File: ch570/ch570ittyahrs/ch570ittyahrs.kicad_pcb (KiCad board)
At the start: 2 copper layers, 0 parts

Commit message: Bump design
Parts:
- added C1: 4.7u, Capacitor_SMD:C_0402_1005Metric, F.Cu at (114.0, 45.3)
- added C10: 0.1μF, Capacitor_SMD:C_0402_1005Metric, F.Cu at (79.9, 59.0)
- added C12: 22μF, Capacitor_SMD:C_0603_1608Metric, F.Cu at (73.6, 57.8)
- added C13: 0.1μF, Capacitor_SMD:C_0402_1005Metric, F.Cu at (79.9, 60.9)
- added C14: 22pF, Capacitor_SMD:C_0402_1005Metric, F.Cu at (79.9, 62.9)
- added C2: 4.7u, Capacitor_SMD:C_0402_1005Metric, F.Cu at (77.0, 57.0)
- added C3: 4.7u, Capacitor_SMD:C_0402_1005Metric, F.Cu at (77.0, 59.0)
- added C4: 0.1u, Capacitor_SMD:C_0402_1005Metric, F.Cu at (77.0, 60.9)
- added C5: 0.1u, Capacitor_SMD:C_0402_1005Metric, F.Cu at (77.0, 62.9)
- added C6: 1u, Capacitor_SMD:C_0402_1005Metric, F.Cu at (79.9, 55.0)
- added C7: 22μF, Capacitor_SMD:C_0603_1608Metric, F.Cu at (73.6, 55.3)
- added C8: 0.1μF, Capacitor_SMD:C_0402_1005Metric, F.Cu at (79.9, 57.0)
- added D1: WS2812B, LED_SMD:LED_WS2812B_PLCC4_5.0x5.0mm_P3.2mm, F.Cu at (88.4, 60.7)
- added H1: HOLE, MountingHole:MountingHole_3.2mm_M3_ISO7380_Pad_TopBottom, F.Cu at (96.7, 55.0)
- added J1: SAO, Connector_PinHeader_2.54mm:PinHeader_2x03_P2.54mm_Vertical_SMD, F.Cu at (77.9, 49.2)
- added J2: USB_C_Receptacle_USB2.0_16P, cnhardware:USB_C_MOD_Receptacle_HRO_TYPE-C-31-M-12, F.Cu at (122.0, 38.8)
- added J3: BAT, Connector_PinHeader_2.00mm:PinHeader_1x02_P2.00mm_Vertical, F.Cu at (99.0, 46.4)
- added L1: L, Inductor_SMD:L_0402_1005Metric, F.Cu at (85.8, 52.4)
- added L2: L, Inductor_SMD:L_0402_1005Metric, F.Cu at (85.8, 54.4)
- added R1: R, RF_Antenna:Texas_SWRA117D_2.4GHz_Left, F.Cu at (82.1, 41.4)
- added R10: 33Ω, Resistor_SMD:R_0603_1608Metric, F.Cu at (73.6, 62.8)
- added R2: 5.1k, Resistor_SMD:R_0402_1005Metric, F.Cu at (85.8, 56.4)
- added R3: 5.1k, Resistor_SMD:R_0402_1005Metric, F.Cu at (88.7, 52.4)
- added R4: 5.1k, Resistor_SMD:R_0402_1005Metric, F.Cu at (88.7, 54.4)
- added R5: 5.1k, Resistor_SMD:R_0402_1005Metric, F.Cu at (88.7, 56.4)
- added R6: 5.1k, Resistor_SMD:R_0402_1005Metric, F.Cu at (112.6, 47.5)
- added R7: 5.1k, Resistor_SMD:R_0402_1005Metric, F.Cu at (91.6, 54.4)
- added R8: NP, Resistor_SMD:R_0402_1005Metric, F.Cu at (115.1, 41.0)
- added R9: 33Ω, Resistor_SMD:R_0603_1608Metric, F.Cu at (73.6, 60.3)
- added SW2: TS-1187A-B-A-B, Button_Switch_SMD:SW_SPST_TL3342, F.Cu at (121.3, 48.1)
- added TP1: INT2, TestPoint:TestPoint_Pad_D1.0mm, F.Cu at (95.4, 45.9)
- added TP2: INT1, TestPoint:TestPoint_Pad_D1.0mm, F.Cu at (95.4, 48.9)
- added U1: ~, cnhardware:DFN-6_1.2x1.0mm_P0.4mm, F.Cu at (114.3, 39.6)
- added U2: ~, cnhardware:WLCSP-9-P0.5mm, F.Cu at (114.3, 48.0)
- added U3: QMC6309, Package_BGA:WLP-4_0.83x0.83mm_P0.4mm, F.Cu at (98.4, 39.2)
- added U5: ~, cnhardware:LGA-14_3x2.5mm_P0.5mm_LayoutBorder3x4y_EVEN_PADS, F.Cu at (103.9, 37.9)
- added U7: CH570Q, Package_DFN_QFN:DFN-10-1EP_3x3mm_P0.5mm_EP1.7x2.5mm, F.Cu at (111.3, 41.4)
- added Y2: 32MHz, Crystal:Crystal_SMD_2016-4Pin_2.0x1.6mm, F.Cu at (107.6, 43.9)
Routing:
- net SWCLK: track 0.00 -> 10.7 mm, vias 0 -> 2
- net SWD: track 0.00 -> 8.12 mm, vias 0 -> 2
- net GND: track 0.00 -> 5.34 mm, vias 0 -> 2
- net +5V: track 0.00 -> 4.19 mm
- net Net-(U7-V5): track 0.00 -> 1.82 mm
- net PWRINT: track 0.00 -> 1.74 mm
- net VDD: track 0.00 -> 1.55 mm

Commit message: Bump itty bitty
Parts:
- moved R3 32.0 mm to (116.2, 36.0), turned to 90 degrees
- moved R4 29.5 mm to (110.2, 34.2)
- moved R7 26.2 mm to (116.0, 44.8)
- moved L1 23.7 mm to (103.5, 36.7), turned to -90 degrees
- moved R1 20.7 mm to (102.5, 37.9), turned to 90 degrees
- moved J3 16.4 mm to (115.0, 49.6), turned to -90 degrees
- moved U5 12.2 mm to (108.8, 49.1), turned to -90 degrees
- moved U3 9.90 mm to (107.3, 34.8)
- moved U2 1.64 mm to (115.0, 46.5)
- moved C1 1.64 mm to (114.7, 43.8)
- moved R6 1.64 mm to (113.2, 46.0)

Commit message: Bump design
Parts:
- removed C12: 22μF, Capacitor_SMD:C_0603_1608Metric
- removed H1: HOLE, MountingHole:MountingHole_3.2mm_M3_ISO7380_Pad_TopBottom
- removed J1: SAO, Connector_PinHeader_2.54mm:PinHeader_2x03_P2.54mm_Vertical_SMD
- added C9: 10u, Capacitor_SMD:C_0402_1005Metric, F.Cu at (110.5, 36.3)
- added R11: 22Ω, cnhardware:R_0402_1005Metric_COMPACT, F.Cu at (104.4, 40.1)
- added TP3: SWCLK, TestPoint:TestPoint_Pad_D1.0mm, F.Cu at (111.2, 38.3)
- added TP4: GND, TestPoint:TestPoint_Pad_D1.0mm, F.Cu at (109.5, 39.3)
- C1, C2, C3: value 4.7u -> 10u
- C7: value 22μF -> 10u; footprint Capacitor_SMD:C_0603_1608Metric -> Capacitor_SMD:C_0402_1005Metric
- D1: value WS2812B -> LED; footprint LED_SMD:LED_WS2812B_PLCC4_5.0x5.0mm_P3.2mm -> LED_SMD:LED_0603_1608Metric
- J3: value BAT -> BAT/MX1.25; footprint Connector_PinHeader_2.00mm:PinHeader_1x02_P2.00mm_Vertical -> Connector_Hirose:Hirose_DF13C_CL535-0402-2-51_1x02-1MP_P1.25mm_Vertical
- R10: value 33Ω -> 220Ω; footprint Resistor_SMD:R_0603_1608Metric -> cnhardware:R_0402_1005Metric_COMPACT
- R9: value 33Ω -> 22Ω; footprint Resistor_SMD:R_0603_1608Metric -> cnhardware:R_0402_1005Metric_COMPACT
- TP1: moved to B.Cu
- TP2: value INT1 -> SWD
- U2: value ~ -> AW32001ECSR
- U3: footprint Package_BGA:WLP-4_0.83x0.83mm_P0.4mm -> cnhardware:WLP-4_0.83x0.83mm_P0.4mm
- moved R10 48.6 mm to (114.8, 37.2), turned to -90 degrees
- moved R9 46.1 mm to (112.3, 35.4), turned to 90 degrees
- moved C4 44.6 mm to (118.5, 44.7), turned to 180 degrees
- moved C3 41.9 mm to (116.0, 43.7), turned to -90 degrees
- moved C2 41.3 mm to (116.6, 45.1), turned to 180 degrees
- moved C8 37.7 mm to (111.5, 36.3), turned to -90 degrees
- moved R2 36.6 mm to (120.5, 44.7), turned to 180 degrees
- moved C7 36.6 mm to (106.4, 39.2), turned to 180 degrees
- moved C10 36.3 mm to (112.6, 43.2), turned to -150 degrees
- moved C5 36.3 mm to (104.4, 39.2), turned to 180 degrees
- moved D1 36.1 mm to (114.3, 35.5), turned to 180 degrees
- moved C14 34.5 mm to (109.0, 44.4), turned to 30 degrees
- moved C6 33.9 mm to (112.2, 44.8), turned to 180 degrees
- moved C13 33.7 mm to (106.4, 40.1), turned to 180 degrees
- moved R5 30.8 mm to (110.8, 34.9)
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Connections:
- C1 pad 1: +5V -> VDD
- C3 pad 1: VDD -> +5V
- D1 pad 1: VDD -> GND
- D1 pad 2: unconnected-(D1-DOUT-Pad2) -> Net-(D1-A)
- R10 pad 1: Net-(U5-VDD) -> Net-(D1-A)
- R10 pad 2: VDD -> LED
- TP2 pad 1: Net-(U5-INT1) -> SWD
- U5 pad 4: Net-(U5-INT1) -> unconnected-(U5-INT1-Pad4)
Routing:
- net GND: track 5.34 -> 92.5 mm, vias 2 -> 13
- net VDD: track 1.55 -> 41.5 mm, vias 0 -> 6
- net SDA: track 0.00 -> 27.3 mm, vias 0 -> 3
- net SCL: track 0.00 -> 26.8 mm, vias 0 -> 2
- net PWRINT: track 1.74 -> 17.7 mm, vias 0 -> 2
- net +BATT: track 0.00 -> 14.8 mm, vias 0 -> 2
- net +5V: track 4.19 -> 15.6 mm, vias 0 -> 3
- net Net-(J2-CC1): track 0.00 -> 6.28 mm
- net Net-(U7-XO): track 0.00 -> 5.37 mm
- net Net-(U5-VDD): track 0.00 -> 4.73 mm
- net LED: track 0.00 -> 3.82 mm, vias 0 -> 2
- net Net-(U3-VDD): track 0.00 -> 3.50 mm
- net SWCLK: track 10.7 -> 13.8 mm, vias 2 -> 3
- net Net-(U2-VDD): track 0.00 -> 2.75 mm
- net Net-(U5-INT2): track 0.00 -> 2.65 mm, vias 0 -> 1
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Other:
- board outline added: 24 x 17.5 mm

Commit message: Bump ittyahrs
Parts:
- removed R1: R, RF_Antenna:Texas_SWRA117D_2.4GHz_Left
- TP2, TP3, TP4: moved to B.Cu
- moved TP4 11.2 mm to (120.6, 38.2), turned to 180 degrees
- moved TP3 7.44 mm to (118.6, 38.2), turned to 180 degrees
- moved R4 6.06 mm to (111.2, 38.4), turned to -150 degrees
- moved TP2 3.80 mm to (116.6, 38.2), turned to 180 degrees
- moved R11 2.75 mm to (107.0, 39.1)
- moved C5 2.75 mm to (107.0, 38.1)
- moved C7 2.68 mm to (108.8, 38.1)
- moved C13 2.68 mm to (108.8, 39.1)
- moved TP1 2.53 mm to (108.7, 36.0)
- moved U5 2.53 mm to (108.3, 36.1)
- moved R9 2.32 mm to (114.5, 36.1)
- moved C8 2.27 mm to (113.6, 37.1)
- moved C9 2.22 mm to (112.6, 36.9)
- moved U3 2.22 mm to (111.1, 36.6), turned to 180 degrees
- moved R5 1.90 mm to (112.7, 34.9), turned to 90 degrees
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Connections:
- D1 pad 1: GND -> Net-(D1-K)
- D1 pad 2: Net-(D1-A) -> VDD
- R10 pad 1: Net-(D1-A) -> Net-(D1-K)
- U7 pad 2: Net-(U7-V5) -> unconnected-(U7-V5-Pad2)
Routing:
- net VDD: track 41.5 -> 52.9 mm, vias 6 -> 8
- net GND: track 92.5 -> 102.8 mm, vias 13 -> 15
- net SWCLK: track 13.8 -> 11.1 mm, vias 3 -> 2
- net SCL: track 26.8 -> 28.7 mm, vias 2 -> 3
- net Net-(D1-A): track 1.87 -> 0.00 mm
- net SWD: track 10.6 -> 8.77 mm
- net SDA: track 27.3 -> 28.9 mm, vias 3 -> 4
- net LED: track 3.82 -> 5.37 mm, vias 2 -> 0
- net Net-(D1-K): track 0.00 -> 1.22 mm
- net +5V: track 15.6 -> 16.7 mm
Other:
- outline, holes or cut-outs redrawn
- board text added: "+"
- board text added: "GND"

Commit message: Tweak tinyahrs
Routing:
- net VDD: track 52.9 -> 39.7 mm
- net SCL: track 28.7 -> 20.1 mm, vias 3 -> 4
- net SDA: track 28.9 -> 26.6 mm
- net GND: track 102.8 -> 104.3 mm
- net +BATT: vias 2 -> 3

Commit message: Tweaking board
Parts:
- removed C10: 0.1μF, Capacitor_SMD:C_0402_1005Metric
- removed R7: 5.1k, Resistor_SMD:R_0402_1005Metric
- added R1: R, RF_Antenna:Texas_SWRA117D_2.4GHz_Right, F.Cu at (98.3, 47.7)
- added TP5: GND, TestPoint:TestPoint_Pad_D1.0mm, B.Cu at (114.8, 34.5)
- added TP6: PA7, TestPoint:TestPoint_Pad_D1.0mm, B.Cu at (114.8, 36.5)
- added TP7: PWRINT, TestPoint:TestPoint_Pad_D1.0mm, B.Cu at (118.5, 47.3)
- added TP8: VDD, TestPoint:TestPoint_Pad_D1.0mm, B.Cu at (113.0, 35.5)
- added TP9: BATT, TestPoint:TestPoint_Pad_D1.0mm, B.Cu at (112.7, 46.7)
- moved C4 6.16 mm to (112.7, 42.7), turned to -150 degrees
- moved C3 4.95 mm to (120.7, 44.7), turned to 180 degrees
- moved R6 4.73 mm to (118.8, 44.7), turned to 180 degrees
- moved R2 2.36 mm to (122.8, 44.7), turned to 0 degrees
- moved U2 0.69 mm to (114.7, 43.8), turned to -120 degrees
- moved C2 0.40 mm to (117.0, 44.6), turned to 0 degrees
- moved C6 0.21 mm to (112.1, 44.2)
- moved C1 0.12 mm to (115.2, 41.6)
- moved R8 0.09 mm to (115.1, 40.4)
- moved L2 0.06 mm to (110.2, 44.3)
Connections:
- R6 pad 2: VDD -> +BATT
- U7 pad 2: unconnected-(U7-V5-Pad2) -> Net-(U7-V5)
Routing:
- net GND: track 104.3 -> 137.2 mm, vias 15 -> 17
- net VDD: track 39.7 -> 34.9 mm, vias 8 -> 6
- net +5V: track 16.7 -> 20.9 mm
- net +BATT: track 14.9 -> 12.3 mm, vias 3 -> 2
- net PWRINT: track 17.8 -> 16.2 mm
- net LED: track 5.37 -> 6.22 mm, vias 0 -> 1
- net Net-(U2-VDD): track 2.75 -> 1.95 mm
- net Net-(J2-CC1): track 6.30 -> 6.97 mm
- net SDA: track 26.6 -> 26.0 mm
- net SCL: track 20.1 -> 19.5 mm

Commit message: Bump designs
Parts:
- removed C14: 22pF, Capacitor_SMD:C_0402_1005Metric
- removed L1, L2: L, Inductor_SMD:L_0402_1005Metric
- removed R1: R, RF_Antenna:Texas_SWRA117D_2.4GHz_Right
- added C15: 1u, Capacitor_SMD:C_0402_1005Metric, F.Cu at (115.8, 43.8)
- added U4: MG6229D4-28, cnhardware:xdfn-reg, F.Cu at (115.7, 42.3)
- TP7: value PWRINT -> GND
- moved TP7 5.37 mm to (113.5, 49.2), turned to -90 degrees
- moved C4 1.12 mm to (113.7, 42.2)
- moved U2 0.99 mm to (113.8, 44.1), turned to -90 degrees
- moved TP9 0.86 mm to (113.5, 47.1)
- moved C6 0.61 mm to (111.5, 44.0), turned to 120 degrees
- moved C1 0.40 mm to (115.3, 41.2), turned to 15 degrees
- moved R11 0.39 mm to (107.4, 39.1)
- moved C13 0.35 mm to (109.2, 39.1)
- moved C5 0.35 mm to (107.3, 38.1)
- moved C7 0.35 mm to (109.2, 38.1)
- moved R3 0.22 mm to (116.0, 37.3)
- moved R4 0.20 mm to (111.4, 38.3)
- moved R8 0.15 mm to (115.0, 40.3)
- moved U1 0.15 mm to (114.3, 39.0)
- moved R10 0.13 mm to (115.9, 35.8)
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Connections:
- R6 pad 2: +BATT -> Net-(U2-VDD)
- TP7 pad 1: PWRINT -> GND
- U2 pad A2: VDD -> Net-(U2-SYS)
- U7 pad 10: Net-(U7-ANT) -> GND
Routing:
- net GND: track 137.2 -> 270.7 mm, vias 17 -> 18
- net Net-(U2-VDD): track 1.95 -> 8.20 mm
- net +BATT: track 12.3 -> 6.60 mm
- net VDD: track 34.9 -> 30.0 mm, vias 6 -> 5
- net Net-(U2-SYS): track 0.00 -> 4.42 mm
- net +5V: track 20.9 -> 23.5 mm
- net Net-(U7-ANT): track 2.46 -> 0.00 mm
- net PWRINT: track 16.2 -> 15.4 mm
- net SCL: track 19.5 -> 18.7 mm
- net Net-(C14-Pad1): track 0.70 -> 0.00 mm
- added copper zone on B.Cu, net GND
- added copper zone on F.Cu, net GND

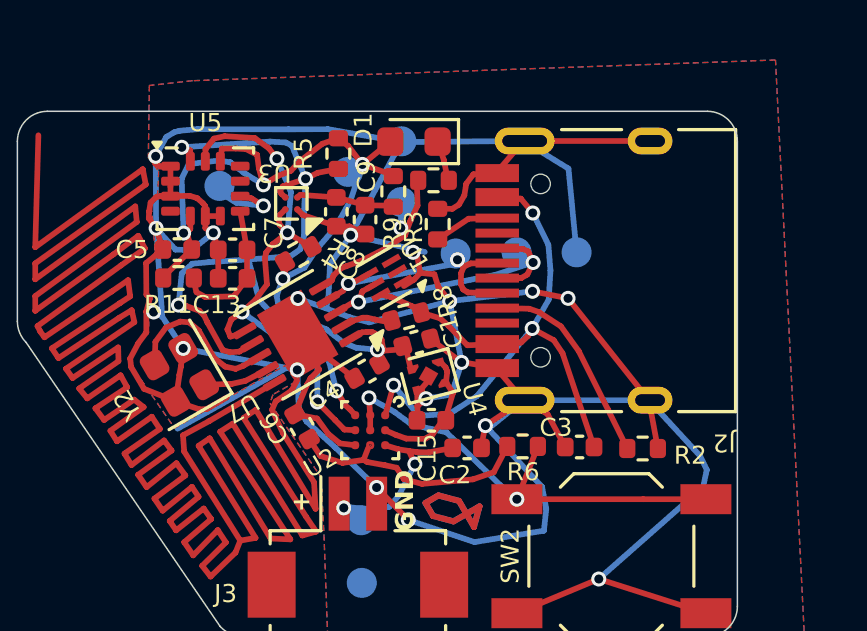
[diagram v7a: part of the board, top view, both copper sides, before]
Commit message: Add some basic test stuff. No QMI yet.
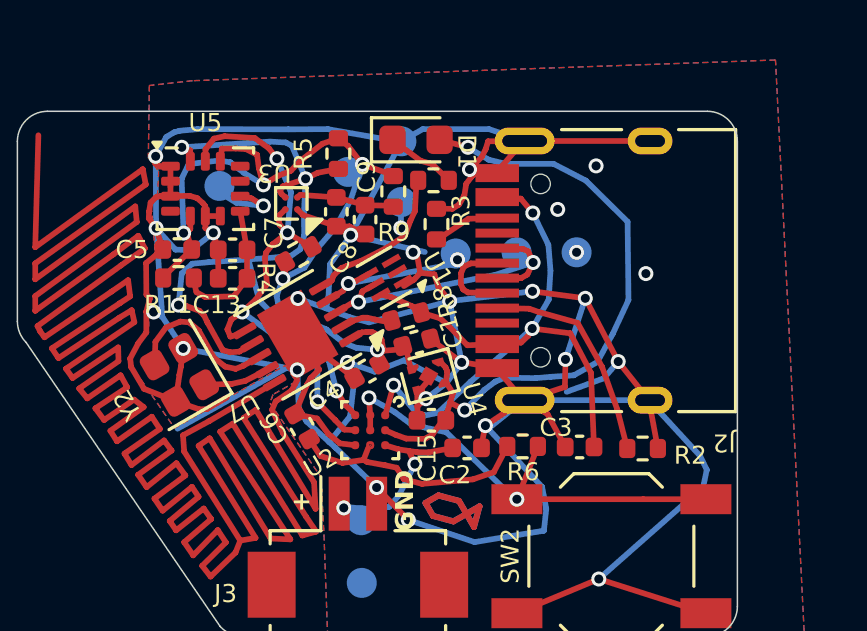
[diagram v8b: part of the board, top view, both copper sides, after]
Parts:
- moved D1 0.09 mm to (115.3, 34.5), turned to 0 degrees
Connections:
- C15 pad 1: Net-(U2-SYS) -> Net-(D1-A)
- D1 pad 2: VDD -> Net-(D1-A)
- U2 pad A2: Net-(U2-SYS) -> Net-(D1-A)
- U4 pad 3: Net-(U2-SYS) -> Net-(D1-A)
- U4 pad 4: Net-(U2-SYS) -> Net-(D1-A)
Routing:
- net Net-(D1-A): track 0.00 -> 22.0 mm, vias 0 -> 2
- net GND: track 270.7 -> 282.6 mm, vias 18 -> 26
- net Net-(U2-SYS): track 4.42 -> 0.00 mm
- net VDD: track 30.0 -> 28.8 mm
- net Net-(D1-K): track 1.22 -> 2.35 mm
